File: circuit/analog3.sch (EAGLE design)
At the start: 75 parts, among them IC1 AD8603UJ, IC2 74HC4052D, IC3 AD8603UJ, IC4 AD8221R, IC5 AD8221R, IC6 LM258, IC7 LM258

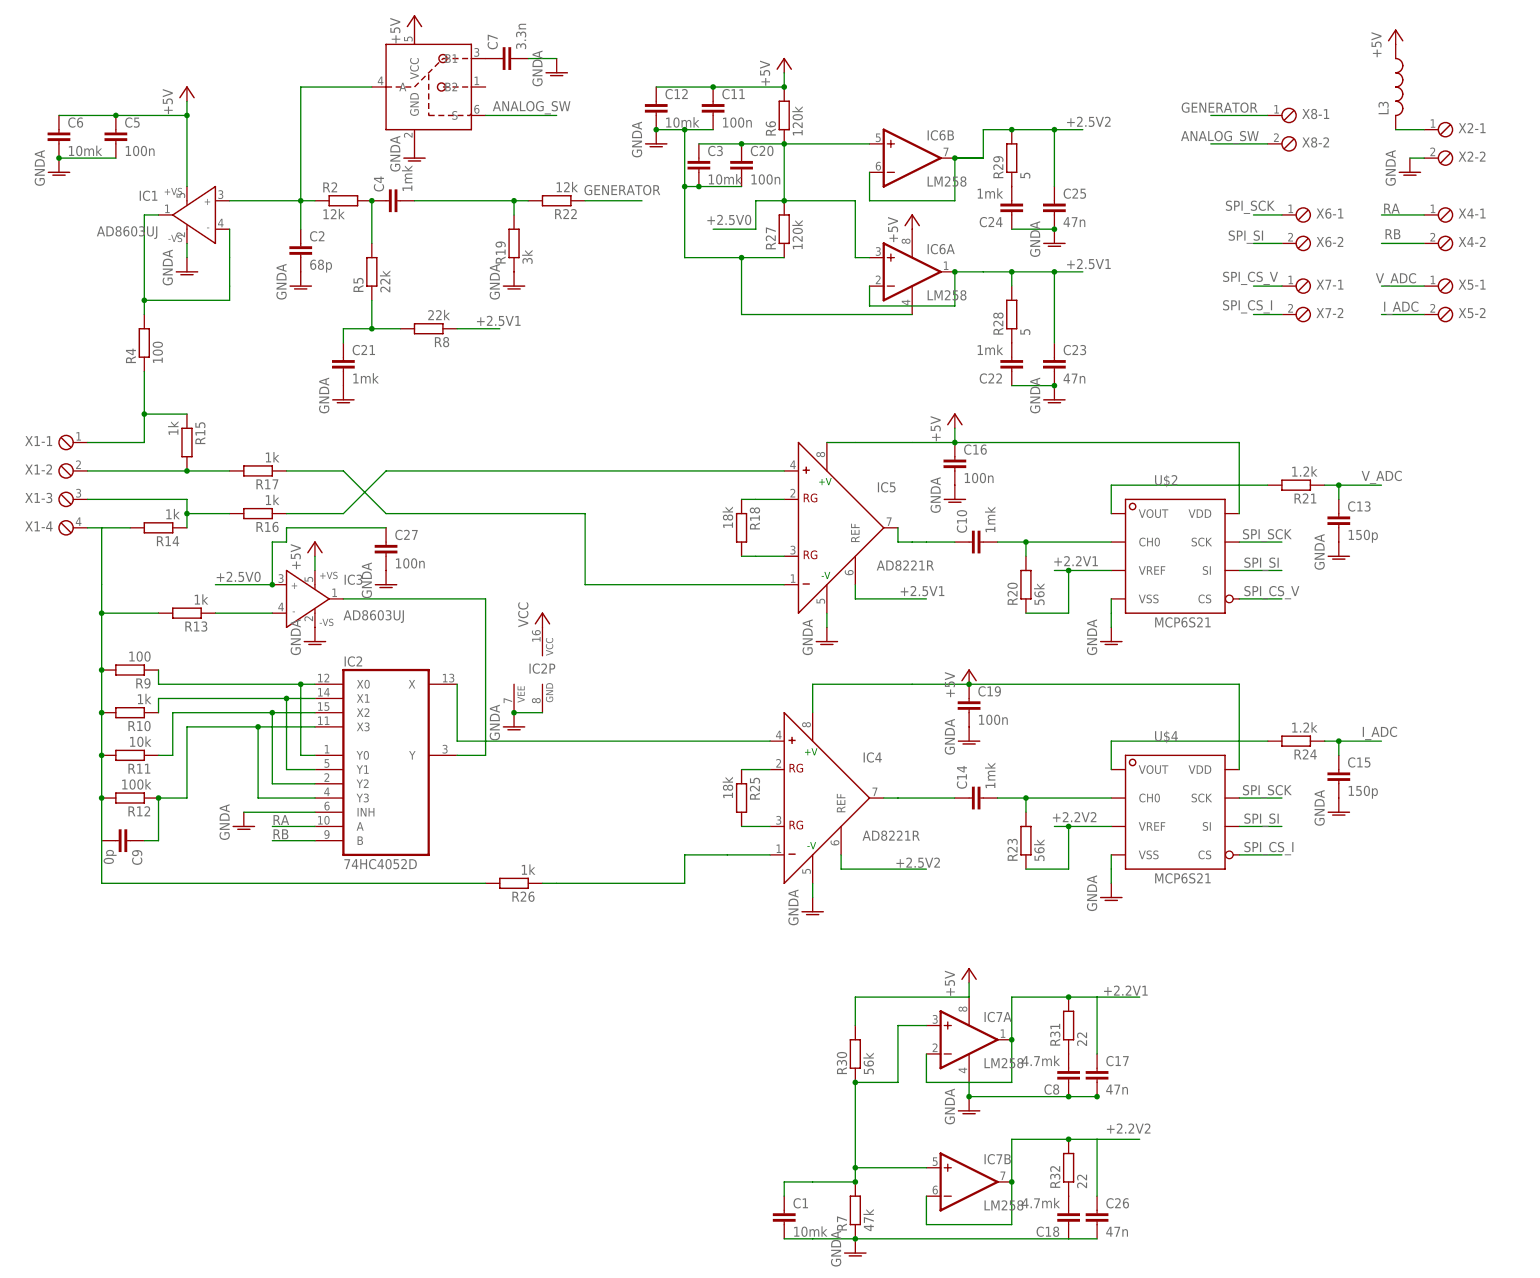
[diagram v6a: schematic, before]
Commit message: - перенесли конденсаторы фильтрующие частоту для ADC на цифровую часть схемы
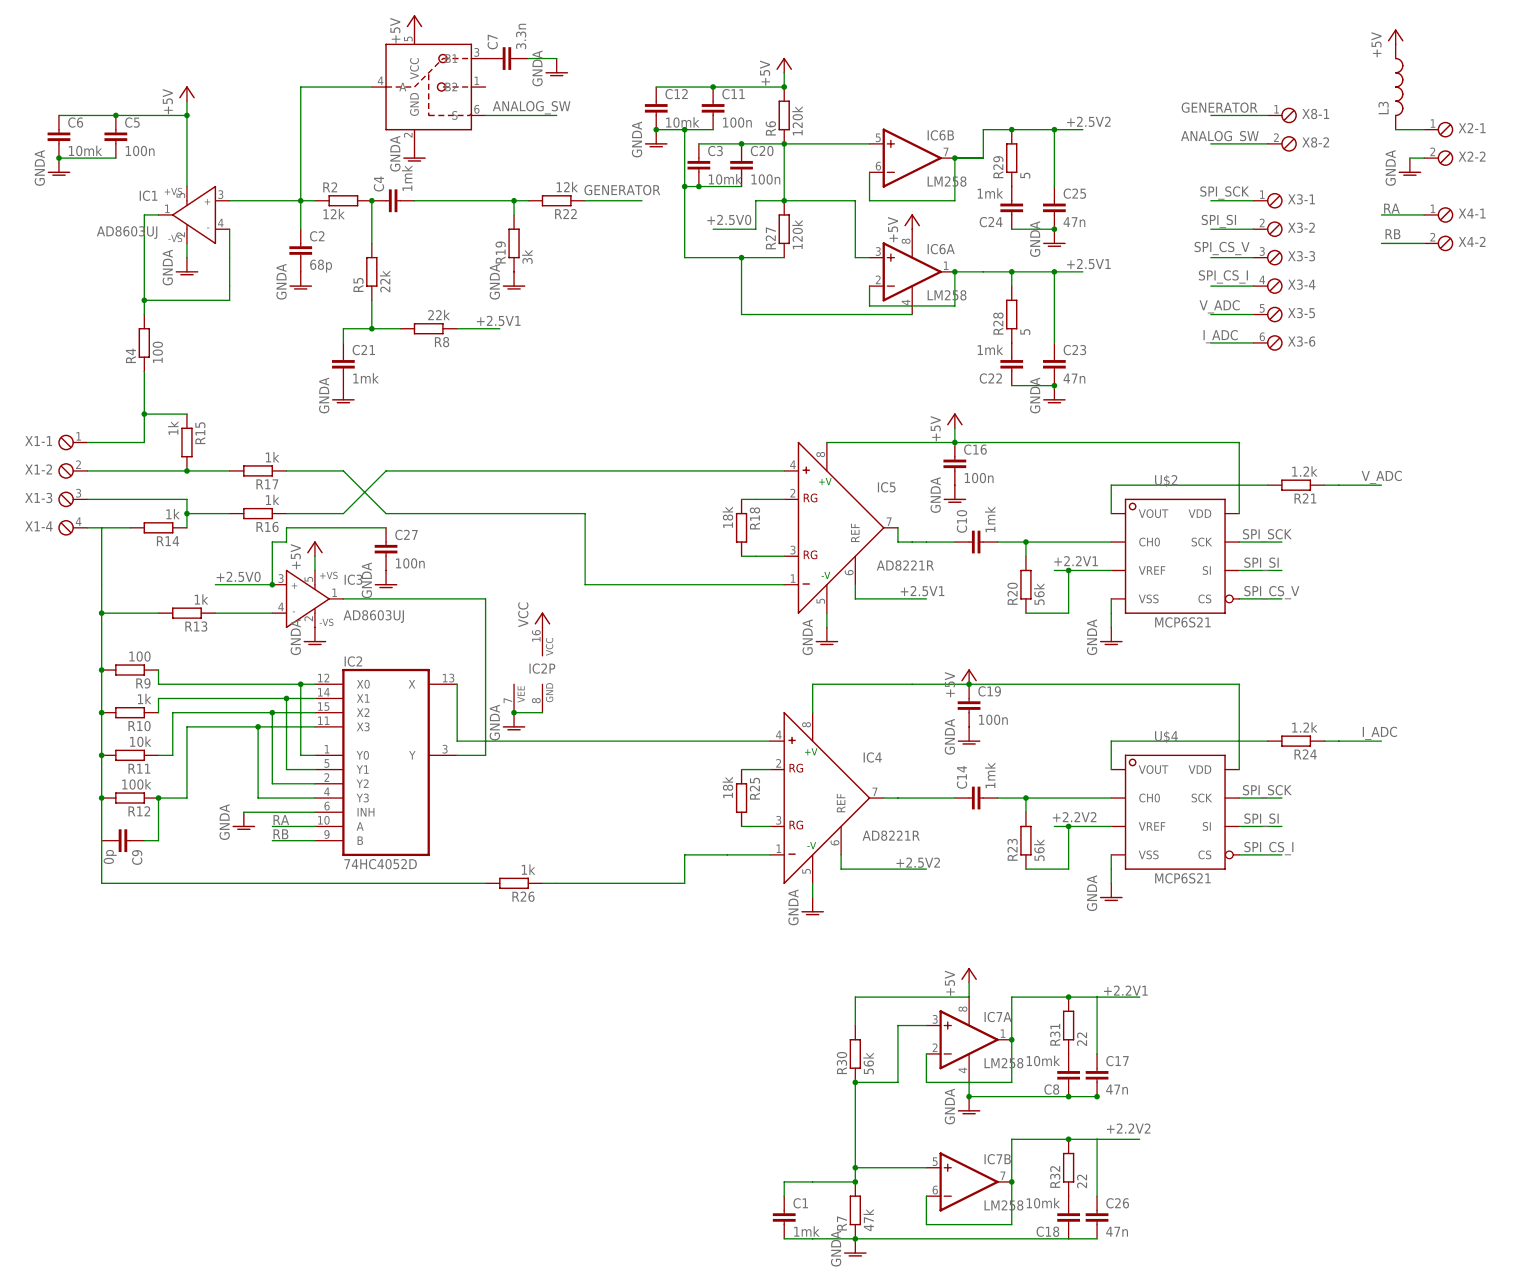
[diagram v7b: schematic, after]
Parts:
- removed C13, C15: 150p, rcl:C-EUC0805
- removed X5, X6, X7: (no value), con-phoenix-254:MPT2
- added X3: (no value), con-phoenix-254:MPT6
- C1: value 10mk -> 1mk; device rcl:C-EUC0805 -> rcl:C-EUC0603
- C18, C8: value 4.7mk -> 10mk; device rcl:C-EUC0603 -> rcl:C-EUC0805
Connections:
- net GNDA: no longer C13.2, C15.2
- net I_ADC: now also X3-6.1; no longer C15.1, X5-2.1
- net SPI_CS_I: now also X3-4.1; no longer X7-2.1
- net SPI_CS_V: now also X3-3.1; no longer X7-1.1
- net SPI_SCK: now also X3-1.1; no longer X6-1.1
- net SPI_SI: now also X3-2.1; no longer X6-2.1
- net V_ADC: now also X3-5.1; no longer C13.1, X5-1.1
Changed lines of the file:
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@@
 <part name="GND11" library="supply1" deviceset="GNDA" device=""/>
 <part name="R21" library="rcl" deviceset="R-EU_" device="R0603" value="1.2k"/>
-<part name="C13" library="rcl" deviceset="C-EU" device="C0805" value="150p"/>
-<part name="GND13" library="supply1" deviceset="GNDA" device=""/>
 <part name="GND14" library="supply1" deviceset="GNDA" device=""/>
 <part name="GND12" library="supply1" deviceset="GNDA" device=""/>
@@
 <part name="GND15" library="supply1" deviceset="GNDA" device=""/>
 <part name="R24" library="rcl" deviceset="R-EU_" device="R0603" value="1.2k"/>
-<part name="C15" library="rcl" deviceset="C-EU" device="C0805" value="150p"/>
-<part name="GND16" library="supply1" deviceset="GNDA" device=""/>
 <part name="R25" library="rcl" deviceset="R-EU_" device="R0603" value="18k"/>
 <part name="R26" library="rcl" deviceset="R-EU_" device="R0603" value="1k"/>
@@
 <part name="X2" library="con-phoenix-254" deviceset="MPT2" device=""/>
 <part name="X4" library="con-phoenix-254" deviceset="MPT2" device=""/>
-<part name="X5" library="con-phoenix-254" deviceset="MPT2" device=""/>
 <part name="P+7" library="supply1" deviceset="+5V" device=""/>
 <part name="GND1" library="supply1" deviceset="GNDA" device=""/>
@@
 <part name="GND3" library="supply1" deviceset="GNDA" device=""/>
 <part name="GND21" library="supply1" deviceset="GNDA" device=""/>
-<part name="X6" library="con-phoenix-254" deviceset="MPT2" device=""/>
-<part name="X7" library="con-phoenix-254" deviceset="MPT2" device=""/>
 <part name="X8" library="con-phoenix-254" deviceset="MPT2" device=""/>
 <part name="C20" library="rcl" deviceset="C-EU" device="C0603" value="100n"/>
@@
 <part name="GND17" library="supply1" deviceset="GNDA" device=""/>
 <part name="R31" library="rcl" deviceset="R-EU_" device="R0805" value="22"/>
-<part name="C8" library="rcl" deviceset="C-EU" device="C0603" value="4.7mk"/>
+<part name="C8" library="rcl" deviceset="C-EU" device="C0805" value="10mk"/>
 <part name="C17" library="rcl" deviceset="C-EU" device="C0805" value="47n"/>
 <part name="R32" library="rcl" deviceset="R-EU_" device="R0805" value="22"/>
-<part name="C18" library="rcl" deviceset="C-EU" device="C0603" value="4.7mk"/>
+<part name="C18" library="rcl" deviceset="C-EU" device="C0805" value="10mk"/>
 <part name="C26" library="rcl" deviceset="C-EU" device="C0805" value="47n"/>
 <part name="GND18" library="supply1" deviceset="GNDA" device=""/>
@@
 <part name="P+8" library="supply1" deviceset="+5V" device=""/>
 <part name="P+9" library="supply1" deviceset="+5V" device=""/>
-<part name="C1" library="rcl" deviceset="C-EU" device="C0805" value="10mk"/>
+<part name="C1" library="rcl" deviceset="C-EU" device="C0603" value="1mk"/>
 <part name="U$1" library="balmer" deviceset="SN74LVC1G3157DBVR" device=""/>
 <part name="GND24" library="supply1" deviceset="GNDA" device=""/>
@@
 <part name="C7" library="rcl" deviceset="C-EU" device="C0805" value="3.3n"/>
 <part name="GND25" library="supply1" deviceset="GNDA" device=""/>
+<part name="X3" library="con-phoenix-254" deviceset="MPT6" device=""/>
 </parts>
 <sheets>
@@
 <instance part="GND11" gate="1" x="15.24" y="-15.24"/>
 <instance part="R21" gate="G$1" x="154.94" y="27.94" rot="R180"/>
-<instance part="C13" gate="G$1" x="162.56" y="22.86"/>
-<instance part="GND13" gate="1" x="162.56" y="15.24"/>
 <instance part="GND14" gate="1" x="-33.02" y="-33.02"/>
 <instance part="GND12" gate="1" x="68.58" y="-48.26"/>
@@
 <instance part="GND15" gate="1" x="121.92" y="-45.72"/>
 <instance part="R24" gate="G$1" x="154.94" y="-17.78" rot="R180"/>
-<instance part="C15" gate="G$1" x="162.56" y="-22.86"/>
-<instance part="GND16" gate="1" x="162.56" y="-30.48"/>
 <instance part="R25" gate="G$1" x="55.88" y="-27.94" rot="R270"/>
 <instance part="R26" gate="G$1" x="15.24" y="-43.18" rot="R180"/>
@@
 <instance part="X4" gate="-1" x="180.34" y="76.2"/>
 <instance part="X4" gate="-2" x="180.34" y="71.12"/>
-<instance part="X5" gate="-1" x="180.34" y="63.5"/>
-<instance part="X5" gate="-2" x="180.34" y="58.42"/>
 <instance part="P+7" gate="1" x="172.72" y="109.22"/>
 <instance part="GND1" gate="1" x="15.24" y="63.5"/>
@@
 <instance part="GND3" gate="1" x="-43.18" y="66.04"/>
 <instance part="GND21" gate="1" x="175.26" y="83.82"/>
-<instance part="X6" gate="-1" x="154.94" y="76.2"/>
-<instance part="X6" gate="-2" x="154.94" y="71.12"/>
-<instance part="X7" gate="-1" x="154.94" y="63.5"/>
-<instance part="X7" gate="-2" x="154.94" y="58.42"/>
 <instance part="X8" gate="-1" x="152.4" y="93.98"/>
 <instance part="X8" gate="-2" x="152.4" y="88.9"/>
@@
 <instance part="C7" gate="G$1" x="12.7" y="104.14" rot="R90"/>
 <instance part="GND25" gate="1" x="22.86" y="101.6"/>
+<instance part="X3" gate="-1" x="149.86" y="78.74"/>
+<instance part="X3" gate="-2" x="149.86" y="73.66"/>
+<instance part="X3" gate="-3" x="149.86" y="68.58"/>
+<instance part="X3" gate="-4" x="149.86" y="63.5"/>
+<instance part="X3" gate="-5" x="149.86" y="58.42"/>
+<instance part="X3" gate="-6" x="149.86" y="53.34"/>
 </instances>
 <busses>
@@
 </segment>
 <segment>
-<pinref part="C13" gate="G$1" pin="2"/>
-<pinref part="GND13" gate="1" pin="GNDA"/>
-</segment>
-<segment>
 <pinref part="IC2" gate="A" pin="INH"/>
 <pinref part="GND14" gate="1" pin="GNDA"/>
@@
 <wire x1="121.92" y1="-43.18" x2="121.92" y2="-40.64" width="0.1524" layer="91"/>
 <wire x1="121.92" y1="-40.64" x2="121.92" y2="-38.1" width="0.1524" layer="91"/>
-</segment>
-<segment>
-<pinref part="C15" gate="G$1" pin="2"/>
-<pinref part="GND16" gate="1" pin="GNDA"/>
 </segment>
 <segment>
@@
 <pinref part="R21" gate="G$1" pin="1"/>
 <wire x1="160.02" y1="27.94" x2="162.56" y2="27.94" width="0.1524" layer="91"/>
-<pinref part="C13" gate="G$1" pin="1"/>
 <wire x1="162.56" y1="27.94" x2="170.18" y2="27.94" width="0.1524" layer="91"/>
-<wire x1="162.56" y1="25.4" x2="162.56" y2="27.94" width="0.1524" layer="91"/>
-<junction x="162.56" y="27.94"/>
 <label x="166.624" y="28.702" size="1.778" layer="95"/>
 </segment>
 <segment>
-<pinref part="X5" gate="-1" pin="1"/>
-<wire x1="177.8" y1="63.5" x2="170.18" y2="63.5" width="0.1524" layer="91"/>
-<label x="169.164" y="64.008" size="1.778" layer="95"/>
+<pinref part="X3" gate="-5" pin="1"/>
+<wire x1="147.32" y1="58.42" x2="139.7" y2="58.42" width="0.1524" layer="91"/>
+<label x="137.668" y="59.182" size="1.778" layer="95"/>
 </segment>
 </net>
@@
 </segment>
 <segment>
-<pinref part="X6" gate="-1" pin="1"/>
-<wire x1="152.4" y1="76.2" x2="147.32" y2="76.2" width="0.1524" layer="91"/>
-<label x="142.24" y="76.962" size="1.778" layer="95"/>
+<pinref part="X3" gate="-1" pin="1"/>
+<wire x1="147.32" y1="78.74" x2="139.7" y2="78.74" width="0.1524" layer="91"/>
+<label x="137.668" y="79.502" size="1.778" layer="95"/>
 </segment>
 </net>
@@
 </segment>
 <segment>
-<pinref part="X6" gate="-2" pin="1"/>
-<wire x1="152.4" y1="71.12" x2="147.32" y2="71.12" width="0.1524" layer="91"/>
-<label x="142.748" y="71.628" size="1.778" layer="95"/>
+<pinref part="X3" gate="-2" pin="1"/>
+<wire x1="147.32" y1="73.66" x2="139.7" y2="73.66" width="0.1524" layer="91"/>
+<label x="137.922" y="74.422" size="1.778" layer="95"/>
 </segment>
 </net>
@@
 </segment>
 <segment>
-<pinref part="X7" gate="-2" pin="1"/>
-<wire x1="152.4" y1="58.42" x2="147.32" y2="58.42" width="0.1524" layer="91"/>
-<label x="141.732" y="59.182" size="1.778" layer="95"/>
+<pinref part="X3" gate="-4" pin="1"/>
+<wire x1="147.32" y1="63.5" x2="139.7" y2="63.5" width="0.1524" layer="91"/>
+<label x="137.414" y="64.516" size="1.778" layer="95"/>
 </segment>
 </net>
@@
 <pinref part="R24" gate="G$1" pin="1"/>
 <wire x1="160.02" y1="-17.78" x2="162.56" y2="-17.78" width="0.1524" layer="91"/>
-<pinref part="C15" gate="G$1" pin="1"/>
 <wire x1="162.56" y1="-17.78" x2="170.18" y2="-17.78" width="0.1524" layer="91"/>
-<wire x1="162.56" y1="-20.32" x2="162.56" y2="-17.78" width="0.1524" layer="91"/>
-<junction x="162.56" y="-17.78"/>
 <label x="166.624" y="-17.018" size="1.778" layer="95"/>
 </segment>
 <segment>
-<pinref part="X5" gate="-2" pin="1"/>
-<wire x1="177.8" y1="58.42" x2="170.18" y2="58.42" width="0.1524" layer="91"/>
-<label x="170.434" y="58.928" size="1.778" layer="95"/>
+<pinref part="X3" gate="-6" pin="1"/>
+<wire x1="147.32" y1="53.34" x2="139.7" y2="53.34" width="0.1524" layer="91"/>
+<label x="138.176" y="53.848" size="1.778" layer="95"/>
 </segment>
 </net>
@@
 </segment>
 <segment>
-<pinref part="X7" gate="-1" pin="1"/>
-<wire x1="152.4" y1="63.5" x2="147.32" y2="63.5" width="0.1524" layer="91"/>
-<label x="141.732" y="64.262" size="1.778" layer="95"/>
-</segment>
-</net>
+<pinref part="X3" gate="-3" pin="1"/>
+<wire x1="147.32" y1="68.58" x2="139.7" y2="68.58" width="0.1524" layer="91"/>
+<label x="136.652" y="69.596" size="1.778" layer="95"/>
+</segment>
+</net>
